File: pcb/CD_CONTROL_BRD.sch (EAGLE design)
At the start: 21 parts, among them SW2 ROTARTY_ENCODER, U1 TC4422AVOA, U2 LCD-16X2SILK

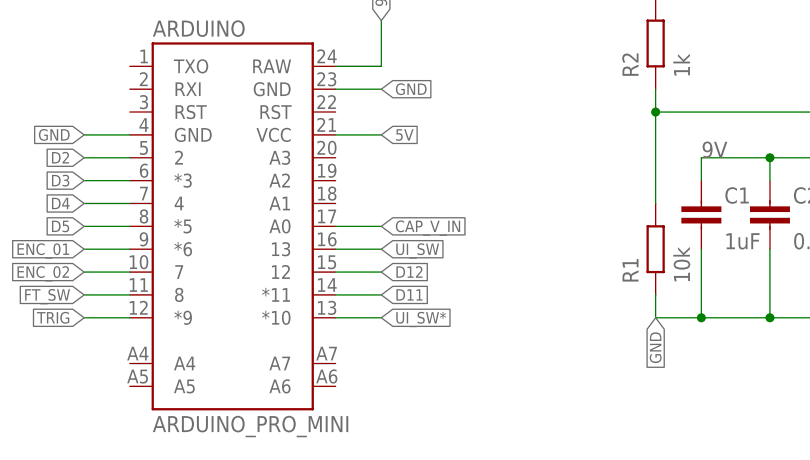
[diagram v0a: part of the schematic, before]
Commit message: finished code. Removed the Diode/Resistor Block...was causing mosfets to latch on
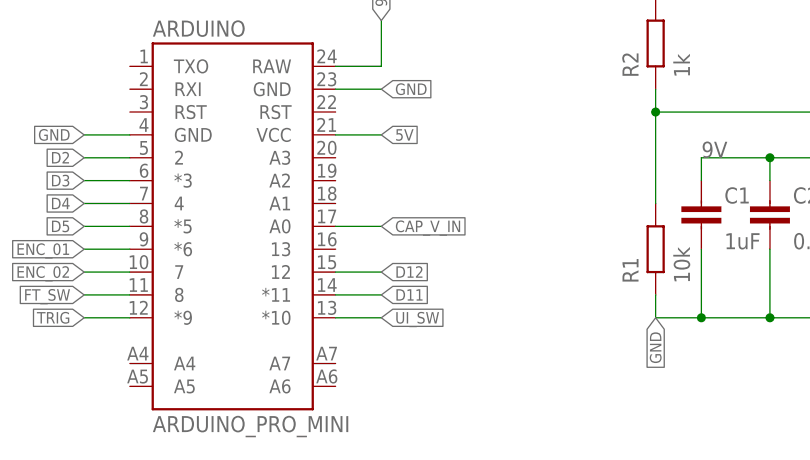
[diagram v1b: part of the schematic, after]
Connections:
- removed net UI_SW*: ARDUINO.*10
- net UI_SW: now also ARDUINO.*10; no longer ARDUINO.13
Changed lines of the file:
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@@
 </segment>
 <segment>
-<pinref part="ARDUINO" gate="G$1" pin="13"/>
-<wire x1="63.5" y1="33.02" x2="68.58" y2="33.02" width="0.1524" layer="91"/>
-<label x="68.58" y="33.02" size="1.27" layer="95" xref="yes"/>
+<pinref part="ARDUINO" gate="G$1" pin="*10"/>
+<wire x1="63.5" y1="25.4" x2="68.58" y2="25.4" width="0.1524" layer="91"/>
+<label x="68.58" y="25.4" size="1.27" layer="95" xref="yes"/>
 </segment>
 </net>
@@
 </segment>
 </net>
-<net name="UI_SW*" class="0">
-<segment>
-<pinref part="ARDUINO" gate="G$1" pin="*10"/>
-<wire x1="63.5" y1="25.4" x2="68.58" y2="25.4" width="0.1524" layer="91"/>
-<label x="68.58" y="25.4" size="1.27" layer="95" xref="yes"/>
-</segment>
-</net>
